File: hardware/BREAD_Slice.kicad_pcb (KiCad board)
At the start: 2 copper layers, 72.6 x 100 mm, 16 parts, among them J1 Conn_01x10_Female, J2 I2C_01x04

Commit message: Initial commit
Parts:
- added C5: 0.01 uF, Capacitor_SMD:C_1206_3216Metric, B.Cu at (165.2, 113.8)
- added C6: 0.01 uF, Capacitor_SMD:C_1206_3216Metric, B.Cu at (165.2, 122.6)
- added D2: General_Purpose_Diode, Diode_THT:D_DO-35_SOD27_P7.62mm_Horizontal, F.Cu at (146.0, 55.3)
- added D3: General_Purpose_Diode, Diode_THT:D_DO-35_SOD27_P7.62mm_Horizontal, F.Cu at (146.0, 81.9)
- added F1: 10A, SparkFun-Fuse:Glass Fuse Clip 5x20MM, F.Cu at (151.1, 72.0)
- added F2: 10A, SparkFun-Fuse:Glass Fuse Clip 5x20MM, F.Cu at (151.1, 45.3)
- added FB1: Ferrite_Bead_Small, Resistor_SMD:R_1206_3216Metric, B.Cu at (170.0, 115.6)
- added FB2: Ferrite_Bead_Small, Resistor_SMD:R_1206_3216Metric, B.Cu at (170.0, 112.1)
- added FB3: Ferrite_Bead_Small, Resistor_SMD:R_1206_3216Metric, B.Cu at (170.0, 124.3)
- added FB4: Ferrite_Bead_Small, Resistor_SMD:R_1206_3216Metric, B.Cu at (170.0, 120.8)
- added J10: Term_PressFit_Phoenix_Contact, SparkFun-Connector:Term_PressFit_5mm_H_PC_HVRELAY, F.Cu at (180.6, 78.7)
- added J11: Term_PressFit_Phoenix_Contact, SparkFun-Connector:Term_PressFit_3.5mm_H_PC, F.Cu at (180.6, 127.7)
- added J12: Term_PressFit_Phoenix_Contact, SparkFun-Connector:Term_PressFit_3.5mm_H_PC, F.Cu at (180.6, 124.2)
- added J13: Term_PressFit_Phoenix_Contact, SparkFun-Connector:Term_PressFit_5mm_H_PC_HVRELAY, F.Cu at (180.6, 83.7)
- added J14: Term_PressFit_Phoenix_Contact, SparkFun-Connector:Term_PressFit_5mm_H_PC_HVRELAY, F.Cu at (180.6, 88.7)
- added J15: Term_PressFit_Phoenix_Contact, SparkFun-Connector:Term_PressFit_5mm_H_PC_HVRELAY, F.Cu at (180.6, 93.7)
- added J16: Term_PressFit_Phoenix_Contact, SparkFun-Connector:Term_PressFit_5mm_H_PC_HVRELAY, F.Cu at (180.6, 98.7)
- added J17: Term_PressFit_Phoenix_Contact, SparkFun-Connector:Term_PressFit_5mm_H_PC_HVRELAY, F.Cu at (180.6, 103.7)
- added J18: Term_PressFit_Phoenix_Contact, SparkFun-Connector:Term_PressFit_5mm_H_PC_HVRELAY, F.Cu at (180.6, 108.7)
- added J3: Term_PressFit_Phoenix_Contact, SparkFun-Connector:Term_PressFit_3.5mm_H_PC, F.Cu at (180.6, 120.7)
- added J4: Term_PressFit_Phoenix_Contact, SparkFun-Connector:Term_PressFit_3.5mm_H_ENDCAP_PC, F.Cu at (180.6, 117.2)
- added J5: Term_PressFit_Phoenix_Contact, SparkFun-Connector:Term_PressFit_5mm_H_ENDCAP_PC_HVRELAY, F.Cu at (180.6, 53.7)
- added J6: Term_PressFit_Phoenix_Contact, SparkFun-Connector:Term_PressFit_5mm_H_PC_HVRELAY, F.Cu at (180.6, 58.7)
- added J7: Term_PressFit_Phoenix_Contact, SparkFun-Connector:Term_PressFit_5mm_H_PC_HVRELAY, F.Cu at (180.6, 63.7)
- added J8: Term_PressFit_Phoenix_Contact, SparkFun-Connector:Term_PressFit_5mm_H_PC_HVRELAY, F.Cu at (180.6, 68.7)
- added J9: Term_PressFit_Phoenix_Contact, SparkFun-Connector:Term_PressFit_5mm_H_PC_HVRELAY, F.Cu at (180.6, 73.7)
- added K1: G5Q-1, Relay_THT:Relay_SPDT_Omron-G5Q-1, F.Cu at (150.0, 62.9)
- added K2: G5Q-1, Relay_THT:Relay_SPDT_Omron-G5Q-1, F.Cu at (150.0, 89.5)
- added U2: TCMT1100, Package_SO:SOP-4_4.4x2.6mm_P1.27mm, B.Cu at (147.6, 66.9)
- added U3: MAX6675ISA+, MAX6675ISA_:SOIC127P600X175-8N, B.Cu at (159.5, 113.8)
- added U4: MAX6675ISA+, MAX6675ISA_:SOIC127P600X175-8N, B.Cu at (159.5, 122.6)
- added U5: TCMT1100, Package_SO:SOP-4_4.4x2.6mm_P1.27mm, B.Cu at (147.6, 93.7)
- moved C1 58.8 mm to (132.5, 60.8)
- moved C2 58.8 mm to (135.1, 67.6)
- moved C3 58.8 mm to (137.8, 60.8)
- moved C4 58.8 mm to (137.8, 57.8)
- moved HS1 58.8 mm to (135.3, 62.7)
- moved L1 58.8 mm to (137.8, 64.1)
- moved U1 58.8 mm to (132.7, 64.1)
- moved A1 7.59 mm to (135.0, 100.0)
- moved J2 7.59 mm to (142.6, 136.4)
- moved Logo1 0.53 mm to (126.4, 72.7)
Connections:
- A1 pad 10: unconnected-(A1-D7-Pad10) -> /Relay2
- A1 pad 13: unconnected-(A1-D10-Pad13) -> /SS1
- A1 pad 14: unconnected-(A1-D11-Pad14) -> /SS2
- A1 pad 15: unconnected-(A1-D12-Pad15) -> /DATA
- A1 pad 16: unconnected-(A1-D13-Pad16) -> /CLK
- A1 pad 9: unconnected-(A1-D6-Pad9) -> /Relay1
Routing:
- net ESTOP2: track 0.00 -> 114.5 mm
- net ESTOP1: track 0.00 -> 111.9 mm
- net /Relay1: track 0.00 -> 61.4 mm
- net /DATA: track 0.00 -> 60.1 mm
- net +12V: track 46.8 -> 102.7 mm
- net IN2: track 0.00 -> 52.8 mm
- net IN1: track 0.00 -> 51.2 mm
- net NC2: track 0.00 -> 40.4 mm
- net NC1: track 0.00 -> 40.2 mm
- net FUSE1: track 0.00 -> 38.1 mm
- net +5V: track 108.9 -> 146.9 mm, vias 1 -> 3
- net FUSE2: track 0.00 -> 37.9 mm
- net NO1: track 0.00 -> 37.3 mm
- net /Relay2: track 0.00 -> 36.8 mm
- net NO2: track 0.00 -> 34.5 mm
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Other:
- board size 72.6 x 100 mm -> 70 x 100 mm
- board text added: "+"
- board text added: "-"
- board text added: "1"
- board text added: "12V->5V Regulator"
- board text added: "2"
- board text added: "BREAD Slice Relay Heating Element Controller SLC_RLHT R2 2024"
- board text added: "E STOP"
- board text added: "IN"
- board text added: "NC"
- board text added: "NO"
- board text added: "RELAY 1"
- board text added: "RELAY 2"
- board text added: "Relay 1"
- board text added: "Relay 2"
- board text added: "THERMOCOUPLES"
- board text added: "Thermocouple 1"
- board text added: "Thermocouple 2"
- board text removed: "12V->5V Reg"
- board text removed: "BREAD Slice Template SLC_TEMP <version> <year>"

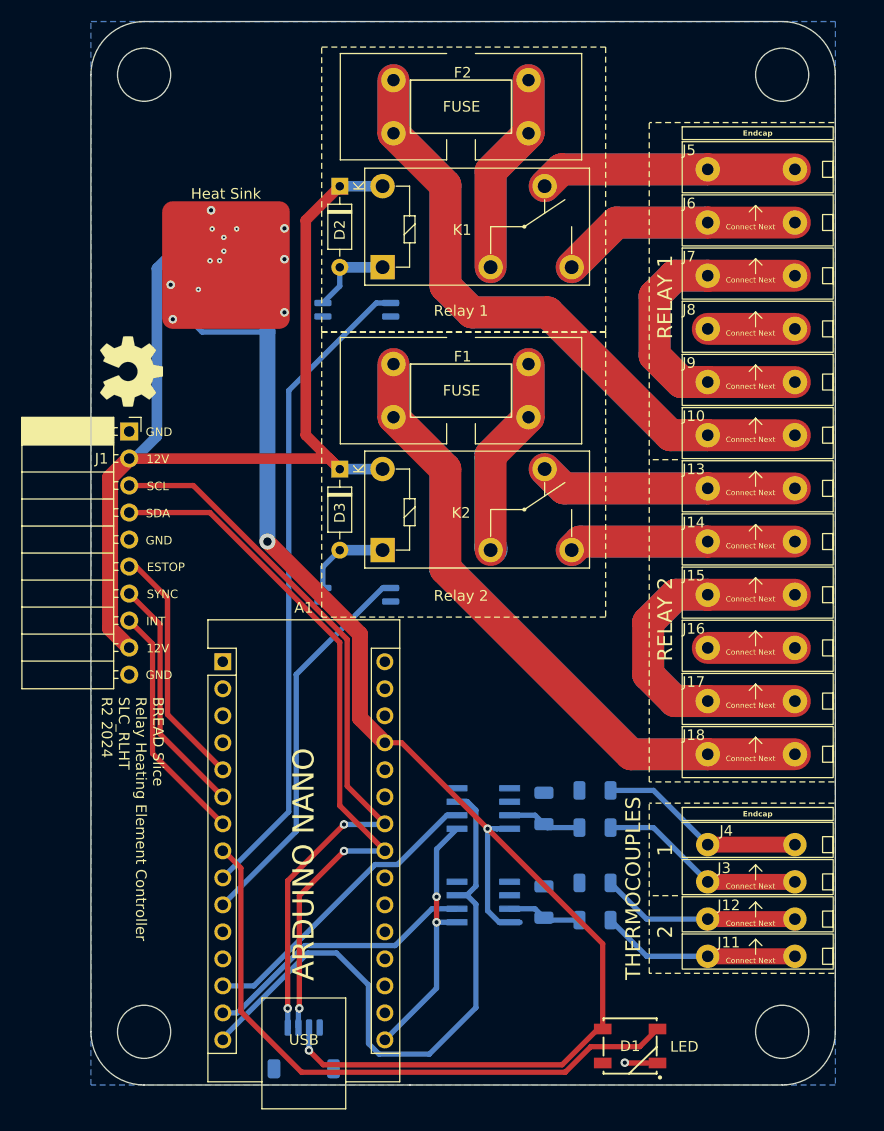
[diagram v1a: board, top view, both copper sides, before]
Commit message: updated to have new terminals and review
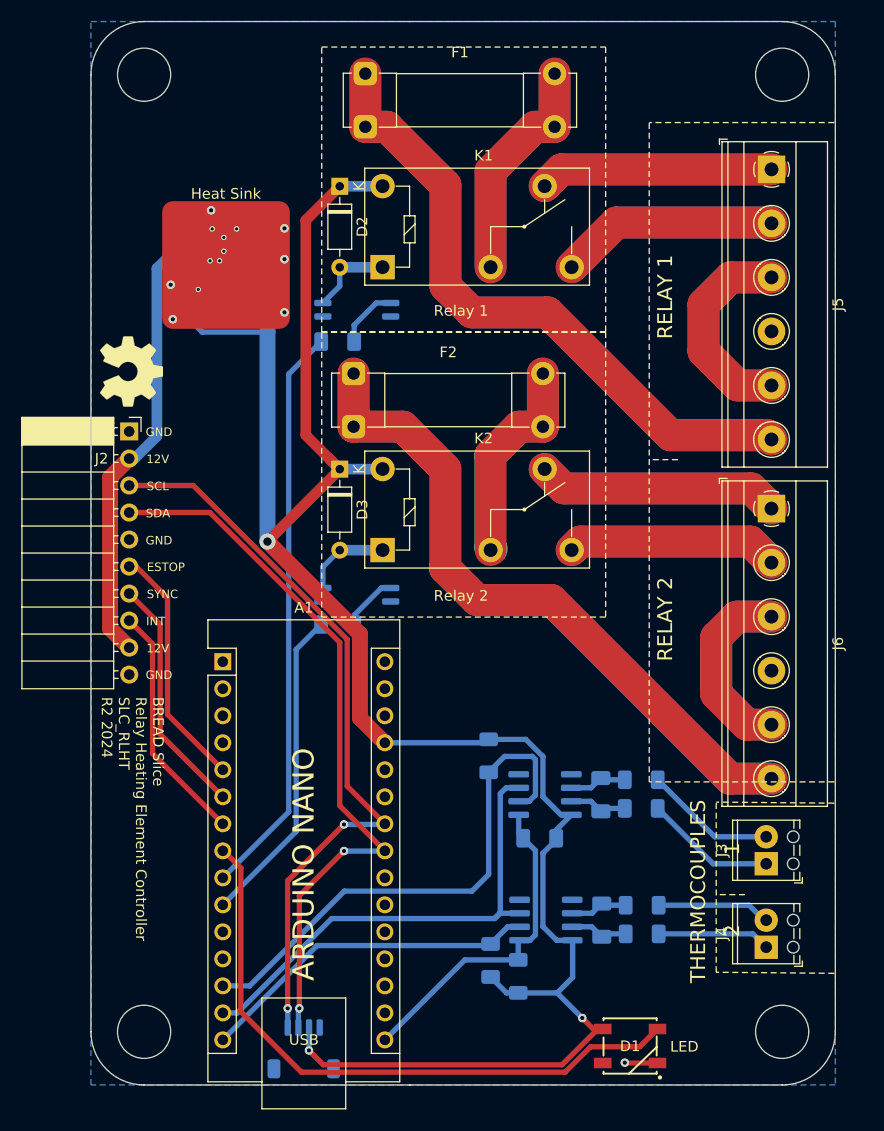
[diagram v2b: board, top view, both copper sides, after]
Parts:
- removed J10, J13, J14, J15, J16, J17, J18, J7, J8, J9: Term_PressFit_Phoenix_Contact, SparkFun-Connector:Term_PressFit_5mm_H_PC_HVRELAY
- removed J11, J12: Term_PressFit_Phoenix_Contact, SparkFun-Connector:Term_PressFit_3.5mm_H_PC
- added R1: 10k, Resistor_SMD:R_1206_3216Metric_Pad1.30x1.75mm_HandSolder, B.Cu at (164.8, 116.6)
- added R2: 10k, Resistor_SMD:R_1206_3216Metric_Pad1.30x1.75mm_HandSolder, B.Cu at (160.0, 108.8)
- added R3: 10k, Resistor_SMD:R_1206_3216Metric_Pad1.30x1.75mm_HandSolder, B.Cu at (162.8, 129.6)
- added R4: 10k, Resistor_SMD:R_1206_3216Metric_Pad1.30x1.75mm_HandSolder, B.Cu at (160.2, 128.1)
- added R5: 180, Resistor_SMD:R_1206_3216Metric_Pad1.30x1.75mm_HandSolder, B.Cu at (145.8, 69.9)
- added R6: 180, Resistor_SMD:R_1206_3216Metric_Pad1.30x1.75mm_HandSolder, B.Cu at (145.8, 96.5)
- C5, C6: footprint Capacitor_SMD:C_1206_3216Metric -> Capacitor_SMD:C_1206_3216Metric_Pad1.33x1.80mm_HandSolder
- D2, D3: value General_Purpose_Diode -> D
- F1, F2: footprint SparkFun-Fuse:Glass Fuse Clip 5x20MM -> Fuse:Fuseholder_Clip-5x20mm_Bel_FC-203-22_Lateral_P17.80x5.00mm_D1.17mm_Horizontal
- FB1, FB2, FB3, FB4: footprint Resistor_SMD:R_1206_3216Metric -> Resistor_SMD:R_1206_3216Metric_Pad1.30x1.75mm_HandSolder
- HS1: footprint SparkFun-Fuse:Thermal Pad -> KML-Custom:Thermal Pad
- J3: value Term_PressFit_Phoenix_Contact -> Screw_Terminal_01x02; footprint SparkFun-Connector:Term_PressFit_3.5mm_H_PC -> TerminalBlock_Phoenix:TerminalBlock_Phoenix_MPT-0,5-2-2.54_1x02_P2.54mm_Horizontal
- J4: value Term_PressFit_Phoenix_Contact -> Screw_Terminal_01x02; footprint SparkFun-Connector:Term_PressFit_3.5mm_H_ENDCAP_PC -> TerminalBlock_Phoenix:TerminalBlock_Phoenix_MPT-0,5-2-2.54_1x02_P2.54mm_Horizontal
- J5: value Term_PressFit_Phoenix_Contact -> Screw_Terminal_01x06; footprint SparkFun-Connector:Term_PressFit_5mm_H_ENDCAP_PC_HVRELAY -> TerminalBlock_Phoenix:TerminalBlock_Phoenix_MKDS-1,5-6-5.08_1x06_P5.08mm_Horizontal
- J6: value Term_PressFit_Phoenix_Contact -> Screw_Terminal_01x06; footprint SparkFun-Connector:Term_PressFit_5mm_H_PC_HVRELAY -> TerminalBlock_Phoenix:TerminalBlock_Phoenix_MKDS-1,5-6-5.08_1x06_P5.08mm_Horizontal
- U2: value TCMT1100 -> MAX31855KASA; footprint Package_SO:SOP-4_4.4x2.6mm_P1.27mm -> Package_SO:SOIC-8_3.9x4.9mm_P1.27mm
- U3: value MAX6675ISA+ -> MAX31855KASA; footprint MAX6675ISA_:SOIC127P600X175-8N -> Package_SO:SOIC-8_3.9x4.9mm_P1.27mm
- U4: value MAX6675ISA+ -> TCMT1100; footprint MAX6675ISA_:SOIC127P600X175-8N -> Package_SO:SOP-4_4.4x2.6mm_P1.27mm
- moved U4 57.0 mm to (147.6, 66.9)
- moved U2 48.9 mm to (165.3, 112.5)
- moved F2 27.8 mm to (147.3, 72.9)
- moved J6 27.6 mm to (186.6, 85.6), turned to -90 degrees
- moved F1 27.4 mm to (148.4, 44.7)
- moved U3 12.0 mm to (165.4, 124.3)
- moved J4 11.1 mm to (186.1, 126.8), turned to 90 degrees
- moved J5 6.00 mm to (186.6, 53.7), turned to -90 degrees
- moved J3 5.76 mm to (186.1, 119.0), turned to 90 degrees
- moved C6 5.69 mm to (170.6, 124.3)
- moved C5 5.51 mm to (170.6, 112.5)
- moved FB4 4.91 mm to (174.4, 122.9)
- moved FB1 4.71 mm to (174.3, 113.8)
- moved FB3 4.62 mm to (174.4, 125.6)
- moved FB2 4.46 mm to (174.3, 111.1)
- renumbered J2 to J1, J1 to J2
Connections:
- net NC1 renamed /Relay/NC
- net Net-(FB1-Pad2) renamed /MAX31855K/T+
- A1 pad 14: /SS2 -> /DATA
- A1 pad 15: /DATA -> /SS2
- C5 pad 1: /T+1 -> Net-(U2-T+)
- C5 pad 2: GND -> Net-(U2-T-)
- C6 pad 1: /T+2 -> Net-(U3-T+)
- C6 pad 2: GND -> Net-(U3-T-)
- D2 pad 1: +12V -> +5V
- D3 pad 1: +12V -> +5V
- F1 pad 1: ESTOP2 -> Net-(J5-Pin_6)
- F1 pad 2: FUSE2 -> /Relay/IN
- F2 pad 1: ESTOP1 -> Net-(J6-Pin_6)
- F2 pad 2: FUSE1 -> /Relay1/IN
- FB1 pad 1: /T+1 -> Net-(U2-T+)
- FB2 pad 1: GND -> Net-(U2-T-)
- FB2 pad 2: Net-(FB2-Pad2) -> /MAX31855K/T-
- FB3 pad 1: /T+2 -> Net-(U3-T+)
- FB3 pad 2: Net-(FB3-Pad2) -> /MAX31855K1/T+
- FB4 pad 1: GND -> Net-(U3-T-)
- FB4 pad 2: Net-(FB4-Pad2) -> /MAX31855K1/T-
- J4 pad 1: Net-(FB2-Pad2) -> /MAX31855K1/T+
- J6 pad 1: NO1 -> /Relay1/NC
- K1 pad 2: FUSE1 -> /Relay/IN
- K1 pad 3: NO1 -> /Relay/NO
- K1 pad 5: +12V -> +5V
- K2 pad 2: FUSE2 -> /Relay1/IN
- K2 pad 3: NO2 -> /Relay1/NO
- K2 pad 4: NC2 -> /Relay1/NC
- K2 pad 5: +12V -> +5V
- U2 pad 1: /Relay1 -> GND
- U2 pad 2: GND -> Net-(U2-T-)
- U2 pad 3: GND -> Net-(U2-T+)
- U2 pad 4: Net-(D2-A) -> +5V
- U3 pad 2: GND -> Net-(U3-T-)
- U3 pad 3: /T+1 -> Net-(U3-T+)
- U3 pad 6: /SS1 -> /SS2
- U3 pad 8: unconnected-(U3-N.C.-Pad8) -> (no net)
- U4 pad 1: GND -> Net-(R5-Pad2)
- U4 pad 3: /T+2 -> GND
- U4 pad 4: +5V -> Net-(D2-A)
- U5 pad 1: /Relay2 -> Net-(R6-Pad2)
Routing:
- net Net-(J6-Pin_6): track 0.00 -> 127.0 mm
- net Net-(J5-Pin_6): track 0.00 -> 121.8 mm
- net ESTOP2: track 114.5 -> 0.00 mm
- net ESTOP1: track 111.9 -> 0.00 mm
- net +12V: track 102.7 -> 45.2 mm
- net +5V: track 146.9 -> 201.5 mm
- net IN2: track 52.8 -> 0.00 mm
- net IN1: track 51.2 -> 0.00 mm
- net /Relay1/NC: track 0.00 -> 45.7 mm
- net /Relay/IN: track 0.00 -> 43.5 mm
- net /Relay/NO: track 0.00 -> 41.1 mm
- net NC2: track 40.4 -> 0.00 mm
- net /Relay1/NO: track 0.00 -> 39.9 mm
- net /Relay1/IN: track 0.00 -> 39.9 mm
- net Net-(J5-Pin_3): track 0.00 -> 39.2 mm
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
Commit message: updated to have new terminals and review
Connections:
- D2 pad 1: +5V -> +12V
- D3 pad 1: +5V -> +12V
- K1 pad 5: +5V -> +12V
- K2 pad 5: +5V -> +12V
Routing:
- net +12V: track 45.2 -> 102.3 mm
- net +5V: track 201.5 -> 153.1 mm

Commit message: JLCPCB order rev-A
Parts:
- added G***: LOGO, LOGO, F.Cu at (166.5, 112.1)
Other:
- board text added: "BREAD Slice Relay Heating Element Controller (SLC_RLHT) Cam K Brooks rev.A [09-2024]"
- board text removed: "BREAD Slice Relay Heating Element Controller SLC_RLHT R2 2024"

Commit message: added historical scripts and new revisions
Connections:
- net /CLK renamed /TC_CLK
- net /DATA renamed /TC_DATA
- net /I2C_CLK renamed /I2C_TC_CLK

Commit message: review and revise for current template and kmlib; still needs updating
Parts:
- removed G***: LOGO, LOGO
- removed the J1 at (142.6, 136.4)
- removed J6: Screw_Terminal_01x06, TerminalBlock_Phoenix:TerminalBlock_Phoenix_MKDS-1,5-6-5.08_1x06_P5.08mm_Horizontal
- added J2: Screw_Terminal_01x02, TerminalBlock_Phoenix:TerminalBlock_Phoenix_MPT-0,5-2-2.54_1x02_P2.54mm_Horizontal, F.Cu at (188.6, 126.0)
- C5, C6: value 0.01 uF -> 10n; moved to F.Cu
- D1: footprint SparkFun-LED:WS2812-5050-4PIN -> KMLib_IC_SMD:WS2812-5050-4PIN
- F1, F2: value 10A -> Fuse
- FB1, FB2, FB3, FB4, R1, R2, R3, R4, U2, U3: moved to F.Cu
- HS1: footprint KML-Custom:Thermal Pad -> KMLib_Mounting:Thermal Pad
- J4: value Screw_Terminal_01x02 -> Screw_Terminal_01x06; footprint TerminalBlock_Phoenix:TerminalBlock_Phoenix_MPT-0,5-2-2.54_1x02_P2.54mm_Horizontal -> TerminalBlock_Phoenix:TerminalBlock_Phoenix_MKDS-1,5-6-5.08_1x06_P5.08mm_Horizontal
- U1: footprint Package_TO_SOT_SMD:TSOT-23-6 -> KMLib_IC_SMD:SOIC_05WU-7_DIO
- moved J5 57.3 mm to (186.6, 111.0), turned to 90 degrees
- moved J4 47.7 mm to (186.6, 79.1)
- moved R2 23.3 mm to (158.4, 132.1), turned to -90 degrees
- moved FB2 18.8 mm to (172.7, 129.9)
- moved F2 18.5 mm to (165.1, 78.0), turned to 180 degrees
- moved F1 18.5 mm to (166.2, 49.7), turned to 180 degrees
- moved R3 18.3 mm to (161.2, 111.4), turned to -90 degrees
- moved U2 16.1 mm to (163.7, 128.5)
- moved C5 16.0 mm to (168.9, 128.5), turned to -90 degrees
- moved R4 15.3 mm to (158.6, 112.9), turned to 90 degrees
- moved FB1 13.5 mm to (172.7, 127.2)
- moved FB3 10.3 mm to (172.8, 115.4)
- moved R1 7.93 mm to (163.2, 124.4)
- moved C6 7.81 mm to (169.0, 116.7), turned to -90 degrees
- moved U3 7.79 mm to (163.8, 116.7)
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- renumbered J2 to J1
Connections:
- A1 pad 13: /SS1 -> /TC_CLK
- A1 pad 14: /TC_DATA -> /SS2
- A1 pad 15: /SS2 -> /TC_DATA
- A1 pad 16: /TC_CLK -> /SS1
- F1 pad 1: Net-(J5-Pin_6) -> /Relay/IN
- F1 pad 2: /Relay/IN -> Net-(J4-Pin_1)
- F2 pad 1: Net-(J6-Pin_6) -> /Relay1/IN
- F2 pad 2: /Relay1/IN -> Net-(J5-Pin_1)
- J3 pad 1: /MAX31855K/T+ -> /MAX31855K1/T-
- J3 pad 2: /MAX31855K/T- -> /MAX31855K1/T+
- J4 pad 1: /MAX31855K1/T+ -> Net-(J4-Pin_1)
- J4 pad 2: /MAX31855K1/T- -> Net-(J4-Pin_2)
- J5 pad 1: /Relay/NC -> Net-(J5-Pin_1)
- J5 pad 2: /Relay/NO -> Net-(J5-Pin_2)
- J5 pad 3: Net-(J5-Pin_3) -> GND
- J5 pad 4: GND -> Net-(J5-Pin_2)
- J5 pad 5: Net-(J5-Pin_3) -> /Relay1/NO
- J5 pad 6: Net-(J5-Pin_6) -> /Relay1/NC
- U2 pad 8: (no net) -> unconnected-(U2-NC-Pad8)
- U3 pad 8: (no net) -> unconnected-(U3-NC-Pad8)
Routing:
- net Net-(J6-Pin_6): track 127.0 -> 0.00 mm
- net Net-(J5-Pin_1): track 0.00 -> 126.9 mm
- net Net-(J5-Pin_6): track 121.8 -> 0.00 mm
- net Net-(J4-Pin_1): track 0.00 -> 121.8 mm
- net Net-(J5-Pin_3): track 39.2 -> 0.00 mm
- net Net-(J4-Pin_2): track 0.00 -> 39.2 mm
- net Net-(J6-Pin_3): track 35.4 -> 0.00 mm
- net Net-(J5-Pin_2): track 0.00 -> 35.4 mm
- net +5V: track 153.1 -> 123.9 mm, vias 3 -> 1
- net /SS1: track 49.4 -> 20.6 mm
- net /I2C_TC_CLK: track 70.5 -> 45.3 mm, vias 2 -> 0
- net /I2C_DAT: track 68.4 -> 46.2 mm, vias 2 -> 0
- net /TC_CLK: track 31.4 -> 49.6 mm
- net /LED: track 59.1 -> 65.9 mm
- net /MAX31855K1/T+: track 10.6 -> 14.7 mm
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- added copper zone on F.Cu, net GND
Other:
- board text added: "BREAD Slice Relay Heating Element Controller (SLC_RLHT) Cam K Brooks rev.B [01-2026]"
- board text removed: "+"
- board text removed: "-"
- board text removed: "1"
- board text removed: "2"
- board text removed: "BREAD Slice Relay Heating Element Controller (SLC_RLHT) Cam K Brooks rev.A [09-2024]"
